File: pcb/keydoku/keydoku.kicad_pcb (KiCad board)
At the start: 2 copper layers, 111 x 99.9 mm, 38 parts

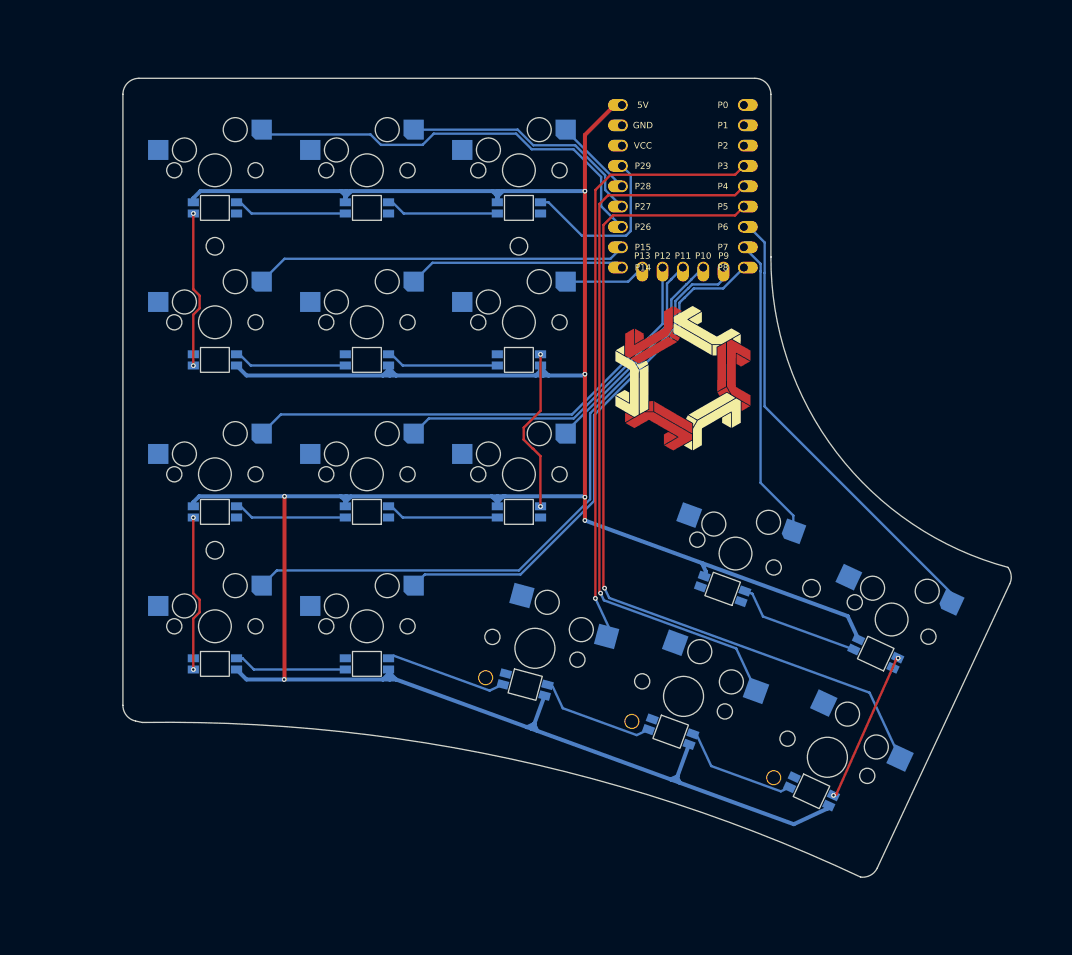
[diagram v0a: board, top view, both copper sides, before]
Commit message: Rounded traces
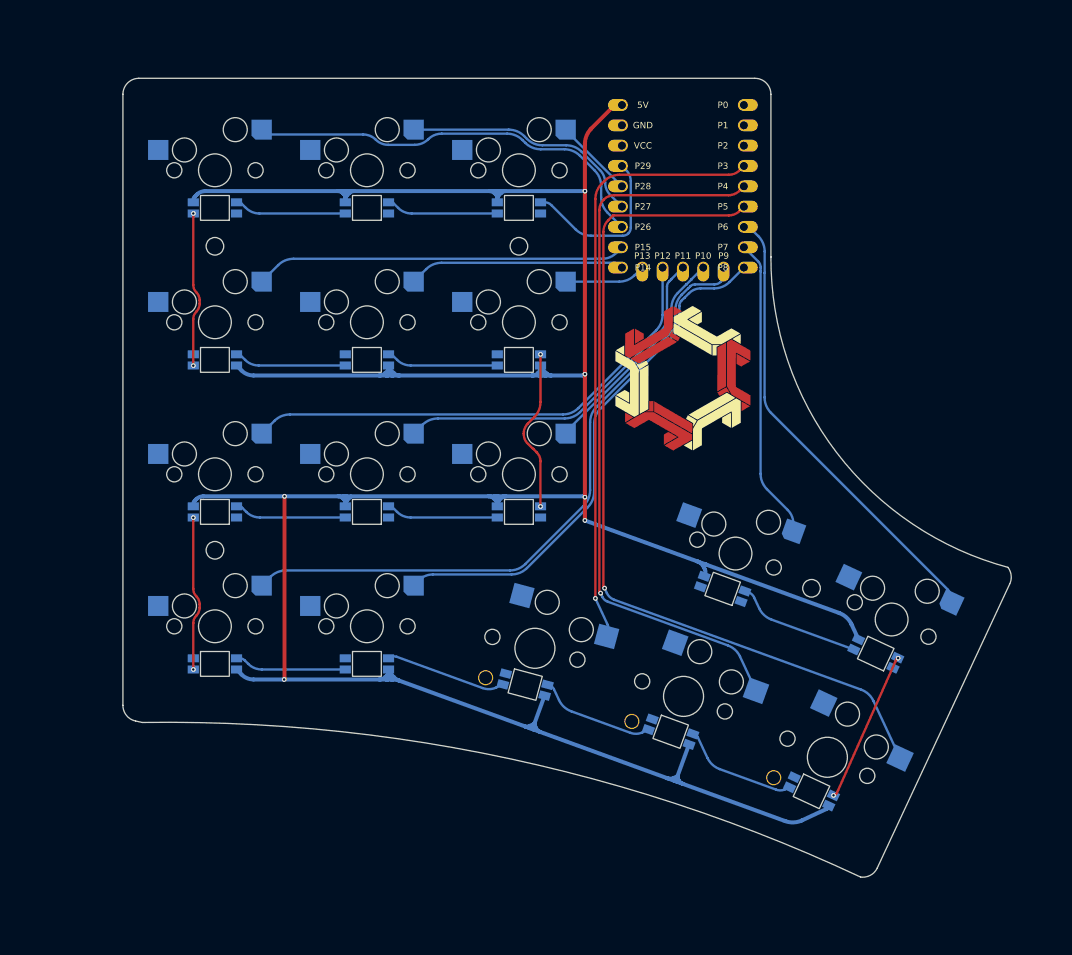
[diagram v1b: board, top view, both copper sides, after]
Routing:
- net VCC5V: track 380.7 -> 395.7 mm
- net P26: track 53.4 -> 52.2 mm
- net P8: track 66.0 -> 65.1 mm
- net P9: track 83.3 -> 82.5 mm
- net P27: track 31.1 -> 30.5 mm

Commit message: PCB complete
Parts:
- moved G*** 2.00 mm to (158.3, 118.1)
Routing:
- net VCC5V: track 395.7 -> 378.5 mm
- net GND: track 0.00 -> 3.43 mm
- net P26: track 52.2 -> 53.4 mm
- net P4: track 91.8 -> 92.8 mm
- net P3: track 75.7 -> 76.6 mm
- net P5: track 108.6 -> 109.5 mm
- net P8: track 65.1 -> 66.0 mm
- net P9: track 82.5 -> 83.3 mm
- net P27: track 30.5 -> 31.1 mm
- added copper zone on B.Cu, net GND
